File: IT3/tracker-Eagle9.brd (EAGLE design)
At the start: 120 x 89.3 mm, 91 parts, among them J1 THING_PLUS_PHYSICAL, Q1 2N3906, Q2 DMG6602SVT, Q3 DMG6602SVT, Q6 MMBT3906LT1SMD, Q7 DMG6602SVT, U1 ADXL343BCCZ-RL7, U2 FONA-800-BREAKOUTNOHOLE, U3 MP2155GQ-Z, U4 SPARKFUN-SWARM-M138NOTOPHOLE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

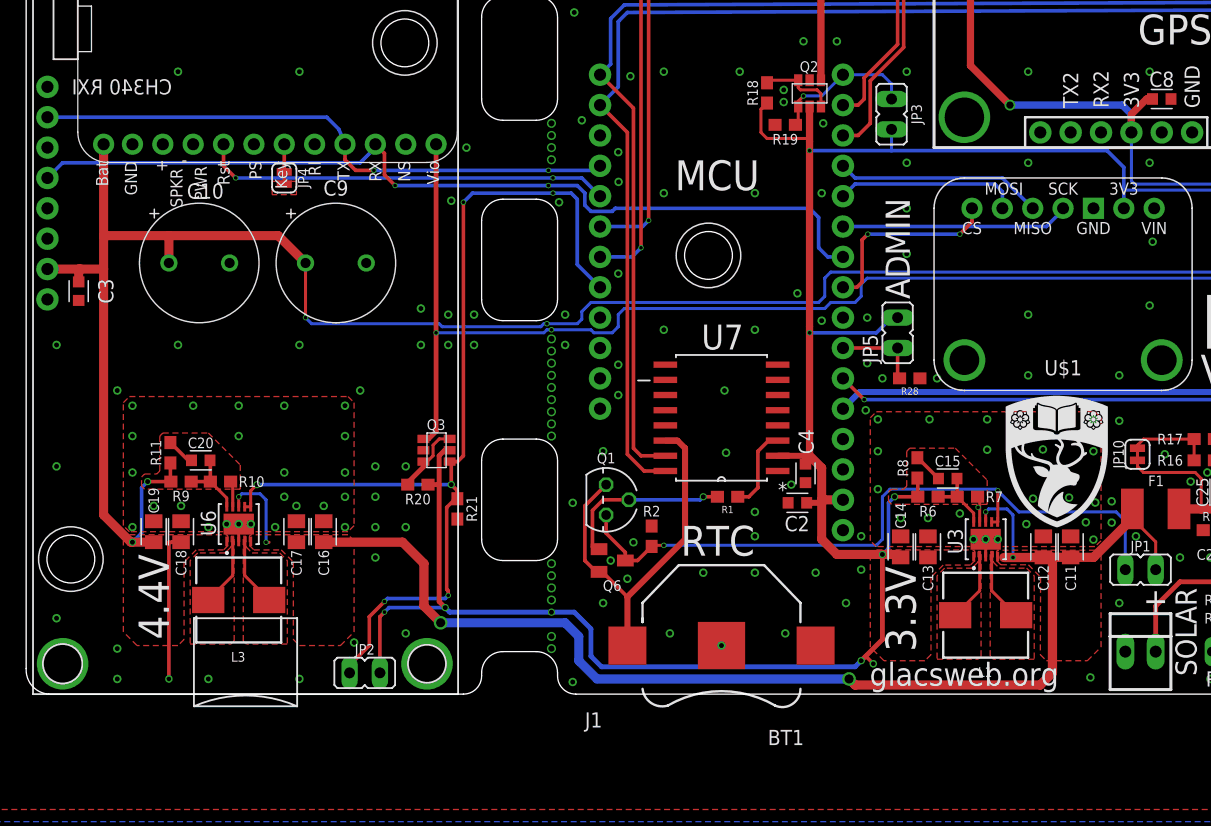
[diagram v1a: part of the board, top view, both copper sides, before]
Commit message: Final silkscreen tweaks and generation of production files
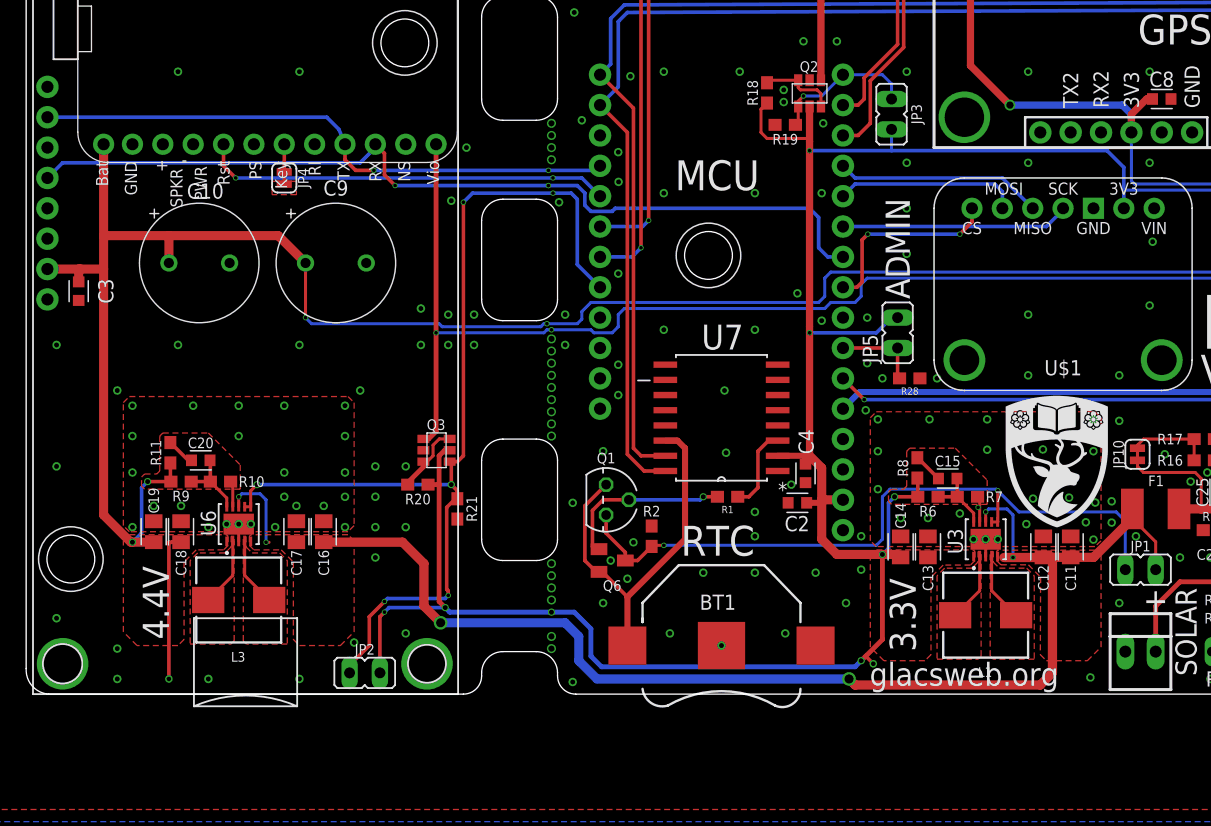
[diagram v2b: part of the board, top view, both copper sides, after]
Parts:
- R10: value 143k -> 100k
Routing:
- net N$31: track 22.9 -> 24.4 mm
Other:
- board text added: "If you can read this, I am broken. Please visit: http://glacsweb.org or mail km@ecs.soton.ac.uk"
- board text removed: "If you can read this, I am broken. Please visit: http://glacsweb.org"
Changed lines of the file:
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@@
 <setting verticaltext="up"/>
 </settings>
-<grid distance="10" unitdist="mil" unit="mil" style="lines" multiple="1" display="yes" altdistance="5" altunitdist="mil" altunit="mil"/>
+<grid distance="50" unitdist="mil" unit="mil" style="lines" multiple="1" display="yes" altdistance="10" altunitdist="mil" altunit="mil"/>
 <layers>
-<layer number="1" name="Top" color="4" fill="1" visible="yes" active="yes"/>
+<layer number="1" name="Top" color="4" fill="1" visible="no" active="yes"/>
 <layer number="2" name="Route2" color="16" fill="1" visible="no" active="no"/>
 <layer number="3" name="Route3" color="17" fill="1" visible="no" active="no"/>
@@
 <layer number="14" name="Route14" color="22" fill="1" visible="no" active="no"/>
 <layer number="15" name="Route15" color="23" fill="1" visible="no" active="no"/>
-<layer number="16" name="Bottom" color="1" fill="1" visible="no" active="yes"/>
+<layer number="16" name="Bottom" color="1" fill="1" visible="yes" active="yes"/>
 <layer number="17" name="Pads" color="2" fill="1" visible="yes" active="yes"/>
 <layer number="18" name="Vias" color="2" fill="1" visible="yes" active="yes"/>
 <layer number="19" name="Unrouted" color="6" fill="1" visible="yes" active="yes"/>
 <layer number="20" name="Dimension" color="24" fill="1" visible="yes" active="yes"/>
-<layer number="21" name="tPlace" color="7" fill="1" visible="yes" active="yes"/>
-<layer number="22" name="bPlace" color="7" fill="1" visible="no" active="yes"/>
-<layer number="23" name="tOrigins" color="15" fill="1" visible="yes" active="yes"/>
-<layer number="24" name="bOrigins" color="15" fill="1" visible="no" active="yes"/>
-<layer number="25" name="tNames" color="7" fill="1" visible="yes" active="yes"/>
-<layer number="26" name="bNames" color="7" fill="1" visible="no" active="yes"/>
+<layer number="21" name="tPlace" color="7" fill="1" visible="no" active="yes"/>
+<layer number="22" name="bPlace" color="7" fill="1" visible="yes" active="yes"/>
+<layer number="23" name="tOrigins" color="15" fill="1" visible="no" active="yes"/>
+<layer number="24" name="bOrigins" color="15" fill="1" visible="yes" active="yes"/>
+<layer number="25" name="tNames" color="7" fill="1" visible="no" active="yes"/>
+<layer number="26" name="bNames" color="7" fill="1" visible="yes" active="yes"/>
 <layer number="27" name="tValues" color="7" fill="1" visible="no" active="yes"/>
 <layer number="28" name="bValues" color="7" fill="1" visible="no" active="yes"/>
@@
 <layer number="37" name="tTest" color="7" fill="1" visible="no" active="yes"/>
 <layer number="38" name="bTest" color="7" fill="1" visible="no" active="yes"/>
-<layer number="39" name="tKeepout" color="4" fill="11" visible="yes" active="yes"/>
-<layer number="40" name="bKeepout" color="1" fill="11" visible="no" active="yes"/>
-<layer number="41" name="tRestrict" color="4" fill="10" visible="yes" active="yes"/>
-<layer number="42" name="bRestrict" color="1" fill="10" visible="no" active="yes"/>
+<layer number="39" name="tKeepout" color="4" fill="11" visible="no" active="yes"/>
+<layer number="40" name="bKeepout" color="1" fill="11" visible="yes" active="yes"/>
+<layer number="41" name="tRestrict" color="4" fill="10" visible="no" active="yes"/>
+<layer number="42" name="bRestrict" color="1" fill="10" visible="yes" active="yes"/>
 <layer number="43" name="vRestrict" color="2" fill="10" visible="no" active="yes"/>
 <layer number="44" name="Drills" color="7" fill="1" visible="no" active="yes"/>
@@
 <layer number="49" name="Reference" color="7" fill="1" visible="no" active="yes"/>
 <layer number="50" name="dxf" color="7" fill="1" visible="no" active="no"/>
-<layer number="51" name="tDocu" color="7" fill="1" visible="yes" active="yes"/>
-<layer number="52" name="bDocu" color="7" fill="1" visible="no" active="yes"/>
+<layer number="51" name="tDocu" color="7" fill="1" visible="no" active="yes"/>
+<layer number="52" name="bDocu" color="7" fill="1" visible="yes" active="yes"/>
 <layer number="53" name="tGND_GNDA" color="7" fill="9" visible="no" active="no"/>
 <layer number="54" name="bGND_GNDA" color="1" fill="9" visible="no" active="no"/>
@@
 <text x="94.488" y="6.858" size="2.032" layer="25" align="bottom-center">+</text>
 <text x="113.03" y="12.7" size="2.032" layer="25" align="bottom-center">+</text>
-<text x="74.422" y="3.556" size="2.54" layer="21" ratio="15" rot="R90">3.3V</text>
-<text x="11.938" y="4.572" size="2.54" layer="21" ratio="15" rot="R90">4.4V</text>
+<text x="74.422" y="3.556" size="2.1844" layer="21" ratio="15" rot="R90">3.3V</text>
+<text x="11.938" y="4.572" size="2.1844" layer="21" ratio="15" rot="R90">4.4V</text>
 <wire x1="44.45" y1="87.776" x2="44.45" y2="87.63" width="0" layer="20"/>
 <wire x1="44.45" y1="76.454" x2="44.45" y2="69.85" width="0" layer="20"/>
@@
 <text x="98.242" y="28.896" size="4.5" layer="25" font="vector" ratio="15">IT3</text>
 <text x="98.242" y="25.848" size="2.54" layer="25" font="vector" ratio="15">V1.0</text>
-<text x="120.221" y="37.388" size="2.1844" layer="22" font="fixed" rot="MR270">Graeme Bragg
+<text x="119.459" y="37.388" size="2.1844" layer="22" font="fixed" rot="MR270">Graeme Bragg
 Kirk Martinez
 Sherif Attia
@@
 <text x="70.556" y="0.702" size="1.9304" layer="25" font="vector" ratio="15">glacsweb.org</text>
 <text x="74.355" y="67.381" size="1.9304" layer="25" font="vector" ratio="15" rot="R90">glacsweb.org</text>
-<text x="82.217" y="1.982" size="2.1844" layer="22" font="fixed" rot="MR90">I am a piece of
+<text x="77.391" y="2.236" size="2.1844" layer="22" font="fixed" rot="MR90">I am a piece of
 scientific equipment
-for glacier monitoring.</text>
-<text x="51.483" y="0.712" size="2.1844" layer="22" font="fixed" rot="MR90">If you can read this,
+for glacier
+monitoring.</text>
+<text x="51.483" y="1.22" size="2.1844" layer="22" font="fixed" rot="MR90">If you can read this,
 I am broken.
 Please visit:
-http://glacsweb.org</text>
+http://glacsweb.org
+or mail km@ecs.soton.ac.uk</text>
 </plain>
 <attributes>
@@
 </class>
 </classes>
-<designrules name="jlcpcb2layer">
+<designrules name="jlcpcb2layer *">
 <description language="en">&lt;b&gt;JLCPCB Design Rules by Jaap de Dood&lt;/b&gt;
 &lt;p&gt;
@@
 <param name="mlMinCreamFrame" value="0mil"/>
 <param name="mlMaxCreamFrame" value="0mil"/>
-<param name="mlViaStopLimit" value="0mil"/>
+<param name="mlViaStopLimit" value="20mil"/>
 <param name="srRoundness" value="0"/>
 <param name="srMinRoundness" value="0mil"/>
@@
 <element name="U5" library="GlacTracker" package="SPARKFUN-GPS-ZED-F9P" value="SPARKFUN-GPS-ZED-F9P" x="119.126" y="45.72" smashed="yes" rot="R90"/>
 <element name="J1" library="SparkFun-Boards" package="THING_PLUS" value="THING_PLUS_PHYSICAL" x="46.736" y="-0.254" smashed="yes">
-<attribute name="NAME" x="46.736" y="-2.794" size="1.27" layer="25" font="vector"/>
 <attribute name="VALUE" x="46.736" y="59.436" size="1.27" layer="27" font="vector"/>
 </element>
@@
 <attribute name="MF" value="Keystone" x="58.166" y="4.064" size="1.778" layer="27" rot="R180" display="off"/>
 <attribute name="MP" value="3000TR" x="58.166" y="4.064" size="1.778" layer="27" rot="R180" display="off"/>
-<attribute name="NAME" x="65.07118125" y="-2.991290625" size="1.27095" layer="25" rot="R180"/>
+<attribute name="NAME" x="56.34081875" y="7.055290625" size="1.27095" layer="25"/>
 <attribute name="PACKAGE" value="None" x="58.166" y="4.064" size="1.778" layer="27" rot="R180" display="off"/>
 <attribute name="PRICE" value="None" x="58.166" y="4.064" size="1.778" layer="27" rot="R180" display="off"/>
@@
 <attribute name="VALUE" x="12.954" y="18.542" size="0.6096" layer="27" font="vector" ratio="20" rot="R180" align="top-center"/>
 </element>
-<element name="R10" library="SparkFun-Resistors" package="0603" value="143k" x="16.256" y="17.78" smashed="yes" rot="R180">
+<element name="R10" library="SparkFun-Resistors" package="0603" value="100k" x="16.256" y="17.78" smashed="yes" rot="R180">
 <attribute name="NAME" x="17.78" y="17.78" size="0.889" layer="25" ratio="20" rot="R180" align="center-right"/>
 <attribute name="PROD_ID" value=" " x="76.708" y="84.836" size="1.778" layer="27" rot="R180" display="off"/>
@@
 <wire x1="26.67" y1="45.974" x2="26.67" y2="44.704" width="0.3048" layer="1"/>
 <wire x1="26.67" y1="44.704" x2="27.559" y2="43.815" width="0.3048" layer="1"/>
-<wire x1="29.083" y1="43.815" x2="27.559" y2="43.815" width="0.3048" layer="1"/>
+<wire x1="27.559" y1="43.815" x2="29.083" y2="43.815" width="0.3048" layer="1"/>
 <wire x1="26.67" y1="45.9994" x2="26.67" y2="45.974" width="0.6096" layer="1"/>
 <via x="43.688" y="43.815" extent="1-16" drill="0.3048"/>
@@
 <wire x1="97.702" y1="21.336" x2="93.472" y2="21.336" width="0.254" layer="1"/>
 <wire x1="92.964" y1="20.828" x2="93.472" y2="21.336" width="0.254" layer="1"/>
-<wire x1="92.964" y1="20.574" x2="92.964" y2="20.828" width="0.254" layer="1"/>
-<wire x1="92.964" y1="19.558" x2="92.964" y2="20.574" width="0.1524" layer="1"/>
+<wire x1="92.964" y1="20.828" x2="92.964" y2="20.574" width="0.254" layer="1"/>
+<wire x1="92.964" y1="19.558" x2="92.964" y2="20.828" width="0.1524" layer="1"/>
 </signal>
 <signal name="N$29">
@@
 <via x="101.346" y="15.494" extent="1-16" drill="0.3048"/>
 <wire x1="92.964" y1="20.574" x2="92.964" y2="19.558" width="0.1524" layer="1"/>
+<wire x1="92.964" y1="20.574" x2="92.964" y2="19.05" width="0.1524" layer="1"/>
 </signal>
 <signal name="GPS_EN">
